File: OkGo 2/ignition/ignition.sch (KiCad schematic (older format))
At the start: 49 parts, among them P101 JST_XH_F, P102 JST_XH_M, P103 CHARGE_CASE, P104 BATT, P105 BATT, P106 SMA, P107 ARM_LED, P108 ARM_LED, P109 BUZZ, P110 BUZZ, P111 SMA, Q101 BSS138BK, SW101 20A ROCKER, U101 CLIP, U102 FUSE 15A, U103 SWD, U104 BEZEL, U105 RFM95W, U106 STM32F071CBT6, U107 TSR 0.5-2433, Y101 8MHz

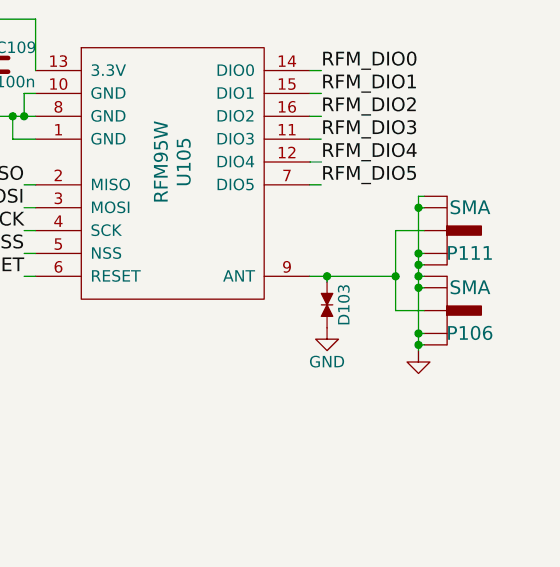
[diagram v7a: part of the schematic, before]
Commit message: Finished footprinting, resolves #9
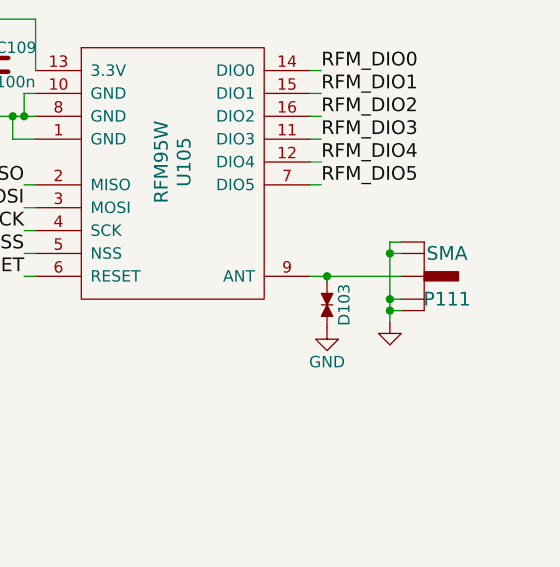
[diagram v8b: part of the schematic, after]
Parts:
- removed P106: SMA, common:SMA-142-0701-801, symbol SMA
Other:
- moved on the sheet: P111
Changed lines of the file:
@@
-$EndComp
-$Comp
-L SMA P106
-U 1 1 559E7125
-P 10600 6200
-F 0 "P106" H 10700 6100 60  0000 C CNN
-F 1 "SMA" H 10700 6300 60  0000 C CNN
-F 2 "common:SMA-142-0701-801" H 10600 6200 60  0001 C CNN
-F 3 "" H 10600 6200 60  0000 C CNN
-F 4 "1342651" H 10600 6200 60  0001 C CNN "Farnell"
-	1    10600 6200
-	1    0    0    -1
 $EndComp
 $Comp
 L GND #PWR118
 U 1 1 559E749A
-P 10475 6375
-F 0 "#PWR118" H 10475 6125 50  0001 C CNN
-F 1 "GND" H 10475 6225 50  0001 C CNN
-F 2 "" H 10475 6375 60  0000 C CNN
-F 3 "" H 10475 6375 60  0000 C CNN
-	1    10475 6375
+P 10350 6250
+F 0 "#PWR118" H 10350 6000 50  0001 C CNN
+F 1 "GND" H 10350 6100 50  0001 C CNN
+F 2 "" H 10350 6250 60  0000 C CNN
+F 3 "" H 10350 6250 60  0000 C CNN
+	1    10350 6250
 	1    0    0    -1
 $EndComp
@@
 L SMA P111
 U 1 1 55D3E20E
-P 10600 5850
-F 0 "P111" H 10700 5750 60  0000 C CNN
-F 1 "SMA" H 10700 5950 60  0000 C CNN
-F 2 "ignition:SMA_upright" H 10600 5850 60  0001 C CNN
-F 3 "http://www.farnell.com/cad/1510251.pdf" H 10600 5850 60  0001 C CNN
-F 4 "2144531" H 10600 5850 60  0001 C CNN "Farnell"
-	1    10600 5850
-	1    0    0    -1
-$EndComp
-Wire Wire Line
-	10500 6350 10475 6350
-Wire Wire Line
-	10475 5700 10475 6375
-Wire Wire Line
-	10500 6300 10475 6300
-Connection ~ 10475 6350
-Wire Wire Line
-	10500 6100 10475 6100
-Connection ~ 10475 6300
-Wire Wire Line
-	10500 6050 10475 6050
-Connection ~ 10475 6100
-Wire Wire Line
-	10500 6000 10475 6000
-Connection ~ 10475 6050
-Wire Wire Line
-	10475 5950 10500 5950
-Connection ~ 10475 6000
-Wire Wire Line
-	10500 5750 10475 5750
-Connection ~ 10475 5950
-Wire Wire Line
-	10500 5700 10475 5700
-Connection ~ 10475 5750
-Wire Wire Line
-	10000 6050 10375 6050
-Wire Wire Line
-	10375 5850 10375 6200
-Wire Wire Line
-	10375 6200 10500 6200
+P 10500 6050
+F 0 "P111" H 10600 5950 60  0000 C CNN
+F 1 "SMA" H 10600 6150 60  0000 C CNN
+F 2 "ignition:SMA_upright" H 10500 6050 60  0001 C CNN
+F 3 "http://www.farnell.com/cad/1510251.pdf" H 10500 6050 60  0001 C CNN
+F 4 "2144531" H 10500 6050 60  0001 C CNN "Farnell"
+	1    10500 6050
+	1    0    0    -1
+$EndComp
 $Comp
 L GND #PWR117
@@
 $EndComp
 Wire Wire Line
-	10500 5850 10375 5850
-Connection ~ 10375 6050
+	10000 6050 10400 6050
+Wire Wire Line
+	10400 6200 10350 6200
+Wire Wire Line
+	10350 5900 10350 6250
+Wire Wire Line
+	10400 6150 10350 6150
+Connection ~ 10350 6200
+Wire Wire Line
+	10400 5950 10350 5950
+Connection ~ 10350 6150
+Wire Wire Line
+	10400 5900 10350 5900
+Connection ~ 10350 5950
 $EndSCHEMATC
